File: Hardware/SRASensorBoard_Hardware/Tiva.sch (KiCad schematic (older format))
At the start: 7 parts, among them U3 TM4C129E_Launchpad

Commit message: rev 2 changes
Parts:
- R3, R4: value 43 -> 130
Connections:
- net NO_Gas: now reaches U3.PD4 (A2_5)
- net NO_Ref: now reaches U3.PD5 (A2_6)
- no-connect marks 52 -> 50
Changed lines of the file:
@@
 Wire Wire Line
 	2000 3400 2175 3400
-Text GLabel 1850 2275 0    50   Output ~ 0
-NO2_SCL
-Text GLabel 1850 2375 0    50   Output ~ 0
-NO2_SDA
-Wire Wire Line
-	2125 2275 1850 2275
-Wire Wire Line
-	2125 2375 1850 2375
 Text GLabel 4000 3500 2    50   Input ~ 0
 TIVA_NH3_A
@@
 NoConn ~ 2125 2075
 NoConn ~ 2175 3200
-NoConn ~ 2175 3500
-NoConn ~ 2175 3600
 NoConn ~ 2175 3700
 NoConn ~ 3825 4000
@@
 NoConn ~ 6975 3825
 NoConn ~ 6975 3925
-$Comp
-L Device:LED D4
-U 1 1 6165658F
-P 1500 4225
-F 0 "D4" H 1475 4125 50  0000 C CNN
-F 1 "Blue" H 1600 4125 50  0000 C CNN
-F 2 "LED_SMD:LED_0603_1608Metric_Pad1.05x0.95mm_HandSolder" H 1500 4225 50  0001 C CNN
-F 3 "~" H 1500 4225 50  0001 C CNN
-	1    1500 4225
-	0    -1   -1   0
-$EndComp
-Wire Wire Line
-	2175 3800 1625 3800
-Wire Wire Line
-	1850 3900 2175 3900
-Wire Wire Line
-	2075 4000 2175 4000
-Wire Wire Line
-	1775 4000 1725 4000
-Wire Wire Line
-	1725 4000 1725 4075
-$Comp
-L Device:R R4
-U 1 1 6165C9F3
-P 1700 3900
-F 0 "R4" V 1600 3975 50  0000 R CNN
-F 1 "43" V 1700 3975 50  0000 R CNN
-F 2 "Resistor_SMD:R_0603_1608Metric_Pad1.05x0.95mm_HandSolder" V 1630 3900 50  0001 C CNN
-F 3 "~" H 1700 3900 50  0001 C CNN
-	1    1700 3900
-	0    -1   -1   0
-$EndComp
-$Comp
-L Device:R R3
-U 1 1 6165CD26
-P 1475 3800
-F 0 "R3" V 1375 3875 50  0000 R CNN
-F 1 "43" V 1475 3875 50  0000 R CNN
-F 2 "Resistor_SMD:R_0603_1608Metric_Pad1.05x0.95mm_HandSolder" V 1405 3800 50  0001 C CNN
-F 3 "~" H 1475 3800 50  0001 C CNN
-	1    1475 3800
-	0    -1   -1   0
-$EndComp
-$Comp
-L Device:LED D3
-U 1 1 616555A2
-P 1275 4225
-F 0 "D3" H 1400 4275 50  0000 C CNN
-F 1 "Blue" H 1525 4275 50  0000 C CNN
-F 2 "LED_SMD:LED_0603_1608Metric_Pad1.05x0.95mm_HandSolder" H 1275 4225 50  0001 C CNN
-F 3 "~" H 1275 4225 50  0001 C CNN
-	1    1275 4225
-	0    -1   -1   0
-$EndComp
-Wire Wire Line
-	1550 3900 1500 3900
-Wire Wire Line
-	1500 3900 1500 4075
-Wire Wire Line
-	1325 3800 1275 3800
-Wire Wire Line
-	1275 3800 1275 4075
-$Comp
-L power:GND #PWR0119
-U 1 1 61666E76
-P 1500 4500
-F 0 "#PWR0119" H 1500 4250 50  0001 C CNN
-F 1 "GND" H 1505 4327 50  0000 C CNN
-F 2 "" H 1500 4500 50  0001 C CNN
-F 3 "" H 1500 4500 50  0001 C CNN
-	1    1500 4500
-	1    0    0    -1
-$EndComp
-$Comp
-L power:GND #PWR0120
-U 1 1 6166AD67
-P 1725 4500
-F 0 "#PWR0120" H 1725 4250 50  0001 C CNN
-F 1 "GND" H 1730 4327 50  0000 C CNN
-F 2 "" H 1725 4500 50  0001 C CNN
-F 3 "" H 1725 4500 50  0001 C CNN
-	1    1725 4500
-	1    0    0    -1
-$EndComp
-$Comp
-L power:GND #PWR0121
-U 1 1 6166AEA5
-P 1275 4500
-F 0 "#PWR0121" H 1275 4250 50  0001 C CNN
-F 1 "GND" H 1280 4327 50  0000 C CNN
-F 2 "" H 1275 4500 50  0001 C CNN
-F 3 "" H 1275 4500 50  0001 C CNN
-	1    1275 4500
-	1    0    0    -1
-$EndComp
-Wire Wire Line
-	1275 4375 1275 4500
-Wire Wire Line
-	1500 4375 1500 4500
-Wire Wire Line
-	1725 4375 1725 4500
 Text Notes 1200 4850 0    50   ~ 0
 Software Signals
@@
 Wire Wire Line
 	3675 1875 3875 1875
+Text GLabel 1975 3500 0    50   Input ~ 0
+NO_Gas
+Text GLabel 1975 3600 0    50   Input ~ 0
+NO_Ref
+Wire Wire Line
+	2175 3500 1975 3500
+Wire Wire Line
+	2175 3600 1975 3600
+$Comp
+L Device:LED D5
+U 1 1 6165680B
+P 1725 4225
+F 0 "D5" H 1675 4125 50  0000 C CNN
+F 1 "Blue" H 1800 4125 50  0000 C CNN
+F 2 "LED_SMD:LED_0603_1608Metric_Pad1.05x0.95mm_HandSolder" H 1725 4225 50  0001 C CNN
+F 3 "~" H 1725 4225 50  0001 C CNN
+	1    1725 4225
+	0    -1   -1   0
+$EndComp
 $Comp
 L Device:R R5
@@
 	0    1    1    0
 $EndComp
-$Comp
-L Device:LED D5
-U 1 1 6165680B
-P 1725 4225
-F 0 "D5" H 1675 4125 50  0000 C CNN
-F 1 "Blue" H 1800 4125 50  0000 C CNN
-F 2 "LED_SMD:LED_0603_1608Metric_Pad1.05x0.95mm_HandSolder" H 1725 4225 50  0001 C CNN
-F 3 "~" H 1725 4225 50  0001 C CNN
-	1    1725 4225
-	0    -1   -1   0
-$EndComp
+Wire Wire Line
+	1725 4375 1725 4500
+Wire Wire Line
+	1500 4375 1500 4500
+Wire Wire Line
+	1275 4375 1275 4500
+$Comp
+L power:GND #PWR0121
+U 1 1 6166AEA5
+P 1275 4500
+F 0 "#PWR0121" H 1275 4250 50  0001 C CNN
+F 1 "GND" H 1280 4327 50  0000 C CNN
+F 2 "" H 1275 4500 50  0001 C CNN
+F 3 "" H 1275 4500 50  0001 C CNN
+	1    1275 4500
+	1    0    0    -1
+$EndComp
+$Comp
+L power:GND #PWR0120
+U 1 1 6166AD67
+P 1725 4500
+F 0 "#PWR0120" H 1725 4250 50  0001 C CNN
+F 1 "GND" H 1730 4327 50  0000 C CNN
+F 2 "" H 1725 4500 50  0001 C CNN
+F 3 "" H 1725 4500 50  0001 C CNN
+	1    1725 4500
+	1    0    0    -1
+$EndComp
+$Comp
+L power:GND #PWR0119
+U 1 1 61666E76
+P 1500 4500
+F 0 "#PWR0119" H 1500 4250 50  0001 C CNN
+F 1 "GND" H 1505 4327 50  0000 C CNN
+F 2 "" H 1500 4500 50  0001 C CNN
+F 3 "" H 1500 4500 50  0001 C CNN
+	1    1500 4500
+	1    0    0    -1
+$EndComp
+Wire Wire Line
+	1275 3800 1275 4075
+Wire Wire Line
+	1325 3800 1275 3800
+Wire Wire Line
+	1500 3900 1500 4075
+Wire Wire Line
+	1550 3900 1500 3900
+$Comp
+L Device:LED D3
+U 1 1 616555A2
+P 1275 4225
+F 0 "D3" H 1400 4275 50  0000 C CNN
+F 1 "Blue" H 1525 4275 50  0000 C CNN
+F 2 "LED_SMD:LED_0603_1608Metric_Pad1.05x0.95mm_HandSolder" H 1275 4225 50  0001 C CNN
+F 3 "~" H 1275 4225 50  0001 C CNN
+	1    1275 4225
+	0    -1   -1   0
+$EndComp
+$Comp
+L Device:R R3
+U 1 1 6165CD26
+P 1475 3800
+F 0 "R3" V 1375 3875 50  0000 R CNN
+F 1 "130" V 1475 3875 50  0000 R CNN
+F 2 "Resistor_SMD:R_0603_1608Metric_Pad1.05x0.95mm_HandSolder" V 1405 3800 50  0001 C CNN
+F 3 "~" H 1475 3800 50  0001 C CNN
+	1    1475 3800
+	0    -1   -1   0
+$EndComp
+Wire Wire Line
+	1725 4000 1725 4075
+Wire Wire Line
+	1775 4000 1725 4000
+Wire Wire Line
+	2075 4000 2175 4000
+Wire Wire Line
+	1850 3900 2175 3900
+Wire Wire Line
+	2175 3800 1625 3800
+$Comp
+L Device:LED D4
+U 1 1 6165658F
+P 1500 4225
+F 0 "D4" H 1475 4125 50  0000 C CNN
+F 1 "Blue" H 1600 4125 50  0000 C CNN
+F 2 "LED_SMD:LED_0603_1608Metric_Pad1.05x0.95mm_HandSolder" H 1500 4225 50  0001 C CNN
+F 3 "~" H 1500 4225 50  0001 C CNN
+	1    1500 4225
+	0    -1   -1   0
+$EndComp
+Text GLabel 1850 2275 0    50   Output ~ 0
+NO2_SCL
+Text GLabel 1850 2375 0    50   Output ~ 0
+NO2_SDA
+Wire Wire Line
+	2125 2275 1850 2275
+Wire Wire Line
+	2125 2375 1850 2375
+$Comp
+L Device:R R4
+U 1 1 6165C9F3
+P 1700 3900
+F 0 "R4" V 1600 3975 50  0000 R CNN
+F 1 "130" V 1700 3975 50  0000 R CNN
+F 2 "Resistor_SMD:R_0603_1608Metric_Pad1.05x0.95mm_HandSolder" V 1630 3900 50  0001 C CNN
+F 3 "~" H 1700 3900 50  0001 C CNN
+	1    1700 3900
+	0    -1   -1   0
+$EndComp

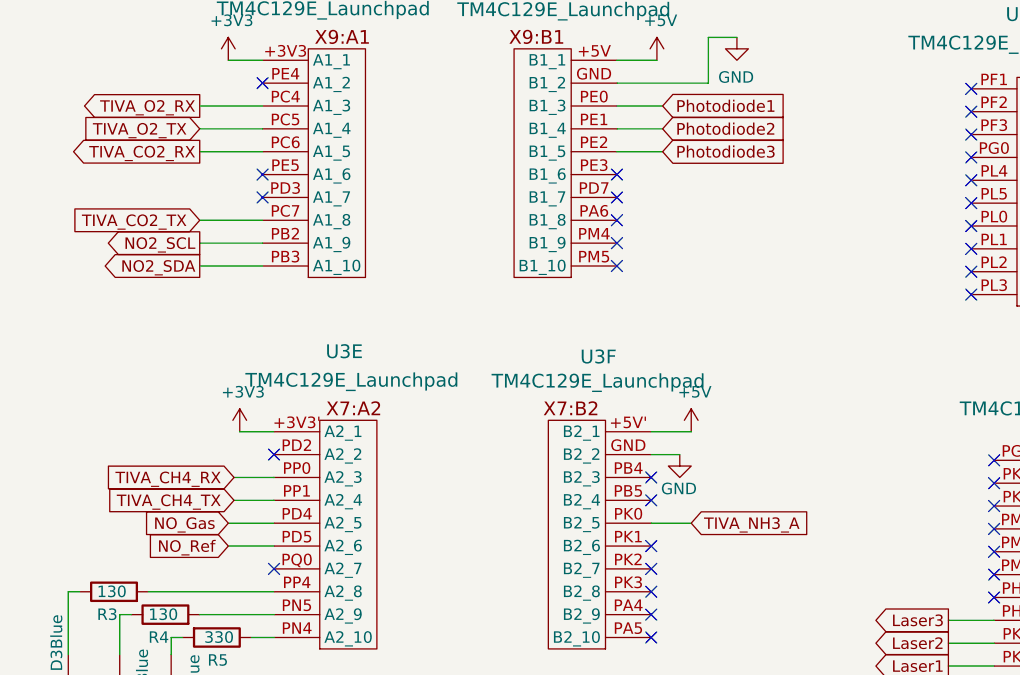
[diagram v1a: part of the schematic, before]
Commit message: added board mounts and did rev 2 changes
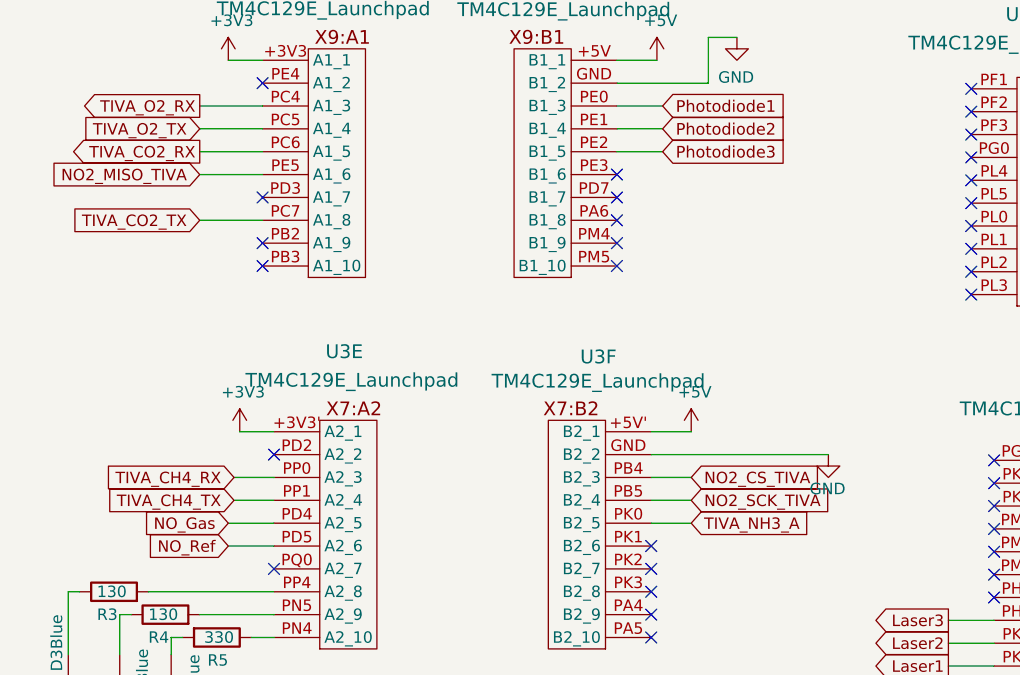
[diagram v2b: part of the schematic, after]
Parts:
- R3, R4, R5: footprint Resistor_SMD:R_0603_1608Metric_Pad1.05x0.95mm_HandSolder -> Resistor_SMD:R_0603_1608Metric_Pad0.98x0.95mm_HandSolder
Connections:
- net NO2_MISO_TIVA: now reaches U3.PE5 (A1_6)
- net NO2_CS_TIVA: now reaches U3.PB4 (B2_3)
- net NO2_SCK_TIVA: now reaches U3.PB5 (B2_4)
- net NO2_SCL: no longer names the net of U3.PB2 (A1_9)
- net NO2_SDA: no longer names the net of U3.PB3 (A1_10)
- no-connect marks 50 -> 49
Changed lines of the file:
@@
 L power:GND #PWR0114
 U 1 1 61501306
-P 3950 3200
-F 0 "#PWR0114" H 3950 2950 50  0001 C CNN
-F 1 "GND" H 4025 3050 50  0000 R CNN
-F 2 "" H 3950 3200 50  0001 C CNN
-F 3 "" H 3950 3200 50  0001 C CNN
-	1    3950 3200
+P 4600 3200
+F 0 "#PWR0114" H 4600 2950 50  0001 C CNN
+F 1 "GND" H 4675 3050 50  0000 R CNN
+F 2 "" H 4600 3200 50  0001 C CNN
+F 3 "" H 4600 3200 50  0001 C CNN
+	1    4600 3200
 	1    0    0    -1
 $EndComp
@@
 Wire Wire Line
 	6975 3225 7100 3225
-Wire Wire Line
-	3825 3200 3950 3200
 $Comp
 L power:+5V #PWR0115
@@
 Wire Wire Line
 	4000 3500 3825 3500
-NoConn ~ 2125 1575
-NoConn ~ 2125 1975
 NoConn ~ 2125 2075
 NoConn ~ 2175 3200
@@
 NoConn ~ 3825 3800
 NoConn ~ 3825 3700
-NoConn ~ 3825 3400
-NoConn ~ 3825 3300
 NoConn ~ 3675 2375
 NoConn ~ 3675 2275
@@
 F 0 "R5" V 2025 4050 50  0000 R CNN
 F 1 "330" V 1925 4075 50  0000 R CNN
-F 2 "Resistor_SMD:R_0603_1608Metric_Pad1.05x0.95mm_HandSolder" V 1855 4000 50  0001 C CNN
+F 2 "Resistor_SMD:R_0603_1608Metric_Pad0.98x0.95mm_HandSolder" V 1855 4000 50  0001 C CNN
 F 3 "~" H 1925 4000 50  0001 C CNN
 	1    1925 4000
@@
 F 0 "R3" V 1375 3875 50  0000 R CNN
 F 1 "130" V 1475 3875 50  0000 R CNN
-F 2 "Resistor_SMD:R_0603_1608Metric_Pad1.05x0.95mm_HandSolder" V 1405 3800 50  0001 C CNN
+F 2 "Resistor_SMD:R_0603_1608Metric_Pad0.98x0.95mm_HandSolder" V 1405 3800 50  0001 C CNN
 F 3 "~" H 1475 3800 50  0001 C CNN
 	1    1475 3800
@@
 	0    -1   -1   0
 $EndComp
-Text GLabel 1850 2275 0    50   Output ~ 0
-NO2_SCL
-Text GLabel 1850 2375 0    50   Output ~ 0
-NO2_SDA
-Wire Wire Line
-	2125 2275 1850 2275
-Wire Wire Line
-	2125 2375 1850 2375
 $Comp
 L Device:R R4
@@
 F 0 "R4" V 1600 3975 50  0000 R CNN
 F 1 "130" V 1700 3975 50  0000 R CNN
-F 2 "Resistor_SMD:R_0603_1608Metric_Pad1.05x0.95mm_HandSolder" V 1630 3900 50  0001 C CNN
+F 2 "Resistor_SMD:R_0603_1608Metric_Pad0.98x0.95mm_HandSolder" V 1630 3900 50  0001 C CNN
 F 3 "~" H 1700 3900 50  0001 C CNN
 	1    1700 3900
 	0    -1   -1   0
 $EndComp
+NoConn ~ 2125 2275
+NoConn ~ 2125 2375
+NoConn ~ 2125 1575
+Text GLabel 1850 1975 0    50   Input ~ 0
+NO2_MISO_TIVA
+Wire Wire Line
+	2125 1975 1850 1975
+Wire Wire Line
+	3825 3200 4600 3200
+Text GLabel 4000 3300 2    50   Input ~ 0
+NO2_CS_TIVA
+Text GLabel 4000 3400 2    50   Input ~ 0
+NO2_SCK_TIVA
+Wire Wire Line
+	4000 3300 3825 3300
+Wire Wire Line
+	4000 3400 3825 3400
 $EndSCHEMATC

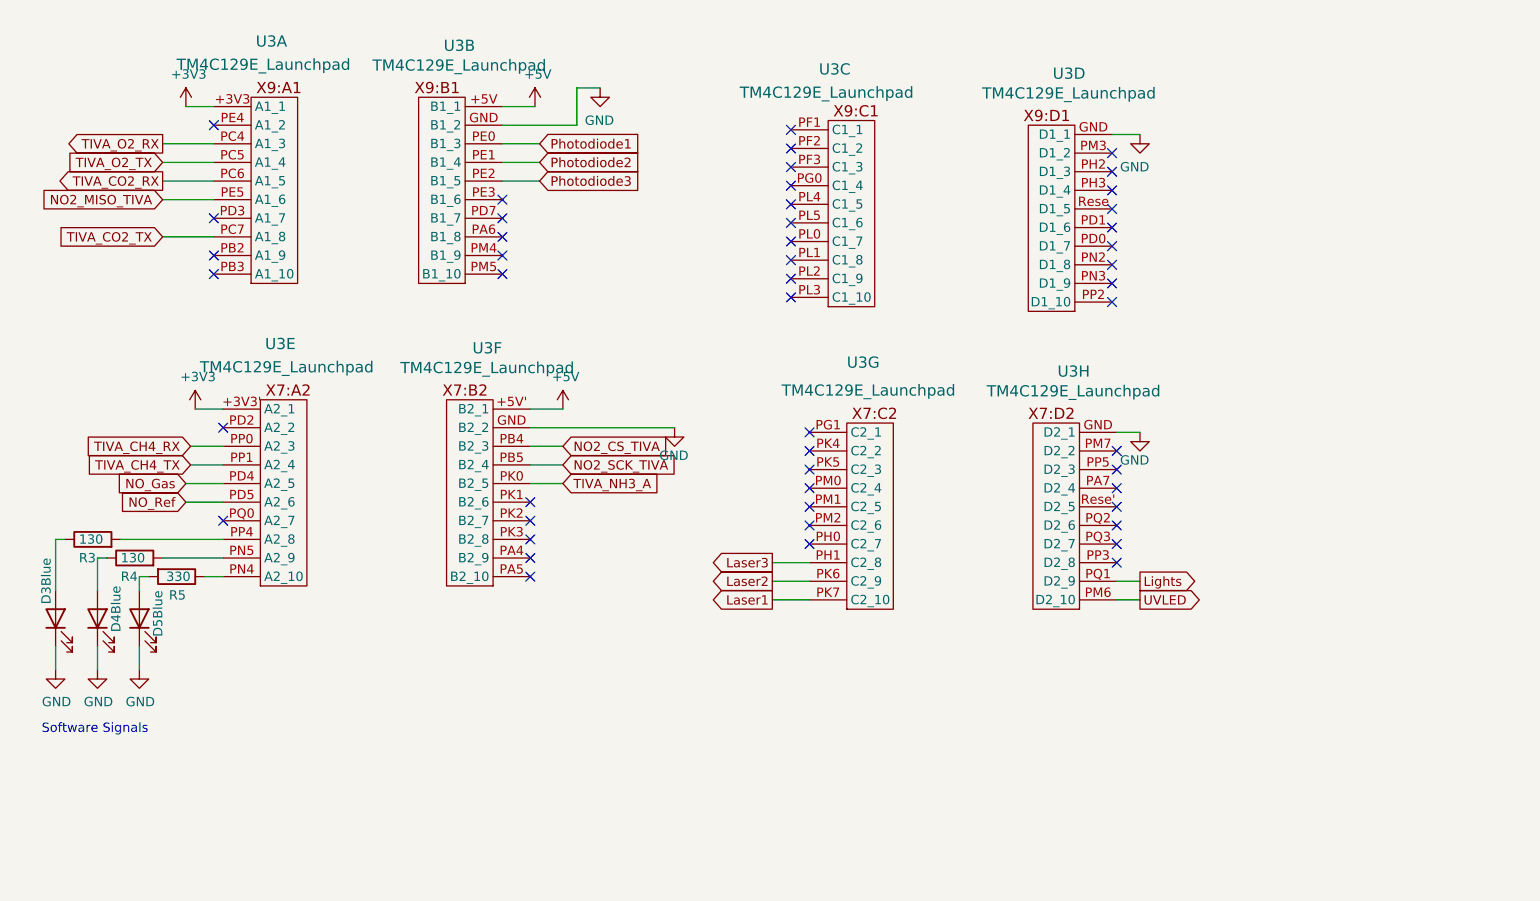
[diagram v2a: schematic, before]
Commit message: added teensy
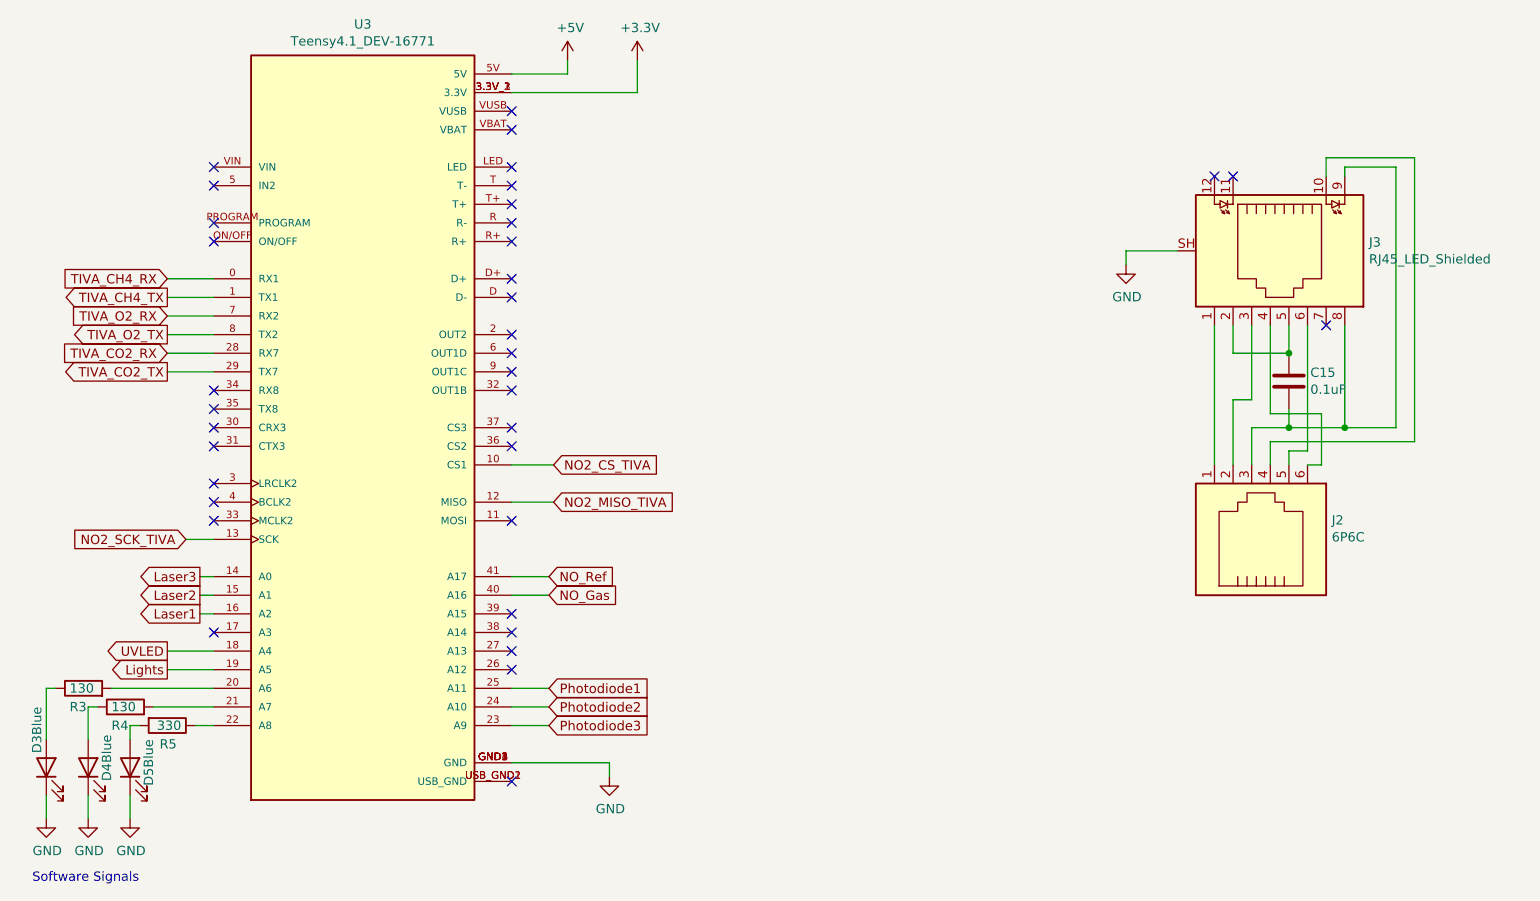
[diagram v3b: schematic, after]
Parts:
- removed U3: TM4C129E_Launchpad, MRDT_Shields:TM4C129E_Launchpad_FULL_Vertical, symbol MRDT_Shields:TM4C129E_Launchpad
- added C15: 0.1uF, Capacitor_SMD:C_0603_1608Metric_Pad1.08x0.95mm_HandSolder, symbol Device:C
- added J2: 6P6C, Connector_PinHeader_2.00mm:PinHeader_2x03_P2.00mm_Vertical, symbol Connector:6P6C
- added J3: RJ45_LED_Shielded, MRDT_Connectors:RJ45_Teensy, symbol Connector:RJ45_LED_Shielded
- added U3: Teensy4.1_DEV-16771, MRDT_Shields:Teensy_4_1_Vertical, symbol MRDT_Shields:Teensy4.1_DEV-16771
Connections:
- net +3V3: now also U3.3.3V_1 (3.3V), U3.3.3V_2 (3.3V), U3.3.3V_3 (3.3V)
- net +5V: now also U3.5V
- net GND: now also J3.SH, U3.GND1 (GND), U3.GND2 (GND), U3.GND3 (GND), U3.GND4 (GND), U3.GND5 (GND)
- net Laser1: now also U3.16 (A2)
- net Laser2: now also U3.15 (A1)
- net Laser3: now also U3.14 (A0)
- net Lights: now also U3.19 (A5)
- net NO2_CS_TIVA: now also U3.10 (CS1)
- net NO2_MISO_TIVA: now also U3.12 (MISO)
- net NO2_SCK_TIVA: now also U3.13 (SCK)
- net NO_Gas: now also U3.40 (A16)
- net NO_Ref: now also U3.41 (A17)
- net Photodiode1: now also U3.25 (A11)
- net Photodiode2: now also U3.24 (A10)
- net Photodiode3: now also U3.23 (A9)
- net TIVA_CH4_RX: now also U3.0 (RX1)
- net TIVA_CH4_TX: now also U3.1 (TX1)
- net TIVA_CO2_RX: now also U3.28 (RX7)
- net TIVA_CO2_TX: now also U3.29 (TX7)
- net TIVA_O2_RX: now also U3.7 (RX2)
- net TIVA_O2_TX: now also U3.8 (TX2)
- net UVLED: now also U3.18 (A4)
- net at R5.1: now also U3.22 (A8)
- net at R4.2: now also U3.21 (A7)
- net at R3.2: now also U3.20 (A6)
- new net: U3.USB_GND1 (USB_GND), U3.USB_GND2 (USB_GND)
- new net: J2.1, J3.1
- new net: J2.4, J3.10
- new net: C15.1, J3.2, J3.5
- new net: J2.2, J3.3
- new net: J2.6, J3.4
- new net: J2.5, J3.6
- new net: C15.2, J2.3, J3.8, J3.9
- no-connect marks 49 -> 36
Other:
- moved on the sheet: D3, D4, D5, R3, R4, R5
